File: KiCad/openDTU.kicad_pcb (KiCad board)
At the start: 4 copper layers, 40 x 50 mm, 54 parts, among them J1 USB_C_Receptacle_USB2.0, J2 Conn_Coaxial, J3 Micro_SD_Card, J4 Conn_02x05_Counter_Clockwise, Q1 BC817, Q2 BC817, SW1 SW_Push, SW2 SW_Push, U1 CH340C, U3 ESP32-WROOM-32, U4 nRF24L01P, U5 NCP1117-3.3_SOT223, Y1 16 MHz

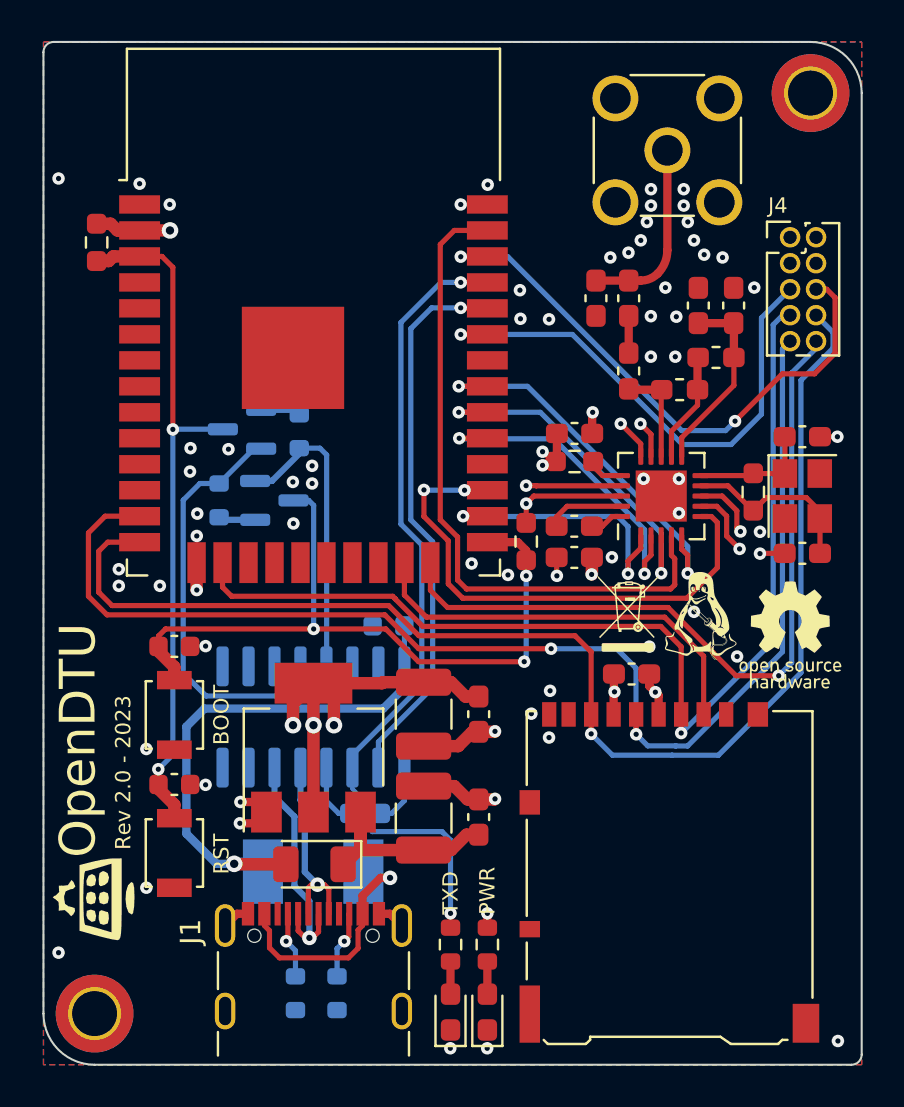
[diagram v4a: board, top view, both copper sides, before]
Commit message: first batch of smt variant ordered
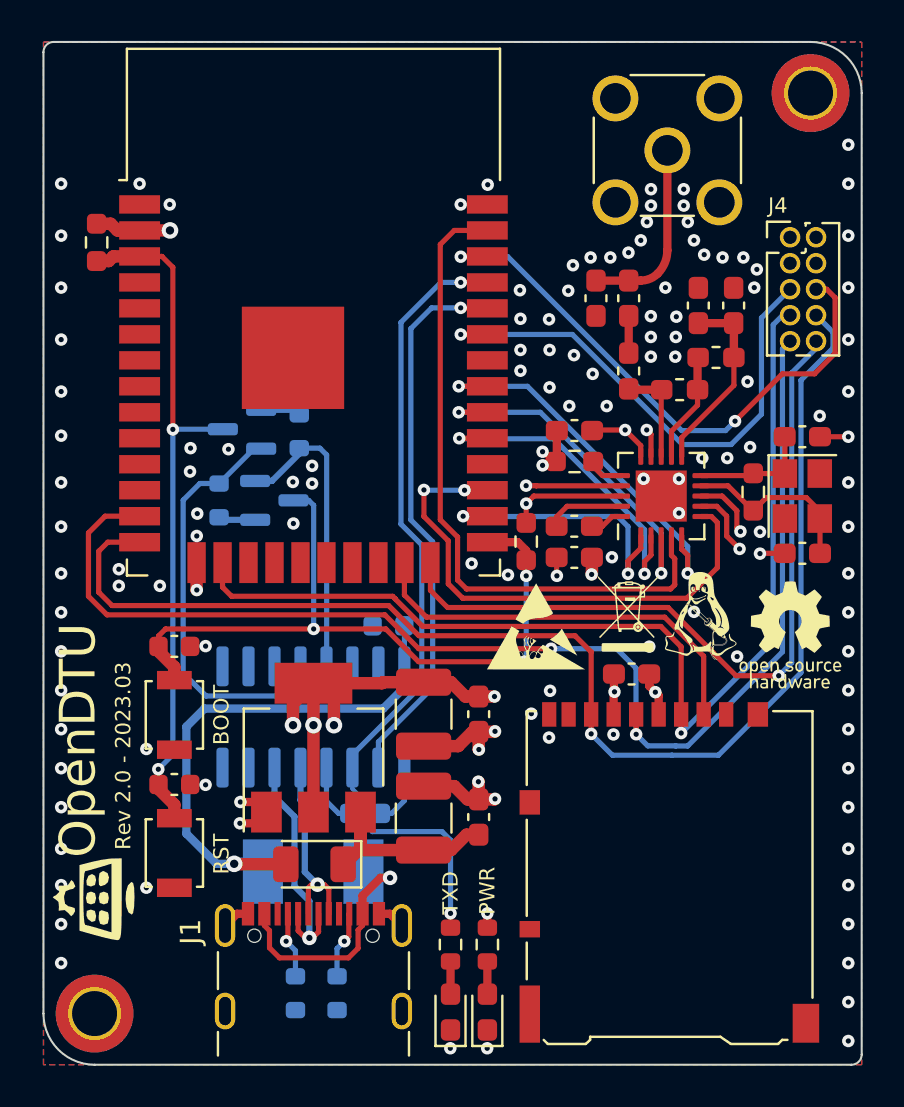
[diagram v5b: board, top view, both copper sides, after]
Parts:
- added G***: LOGO, LOGO, F.Cu at (149.6, 96.6)
- added REF**: KiCad-Logo2_6mm_SilkScreen, Symbol:KiCad-Logo2_6mm_SilkScreen, B.Cu at (154.9, 110.2)
- moved C3 0.14 mm to (151.5, 87.0), turned to 180 degrees
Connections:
- R1 pad 1: +3.3V -> GND
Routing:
- net GND: track 34.9 -> 38.8 mm, vias 72 -> 133
- net +3.3V: track 41.2 -> 40.3 mm, vias 12 -> 11
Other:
- board text added: "Rev 2.0 - 2023.03"
- board text removed: "Rev 2.0 - 2023"

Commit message: fixing bug with wrong voltage at USB-Seriell Interface IC
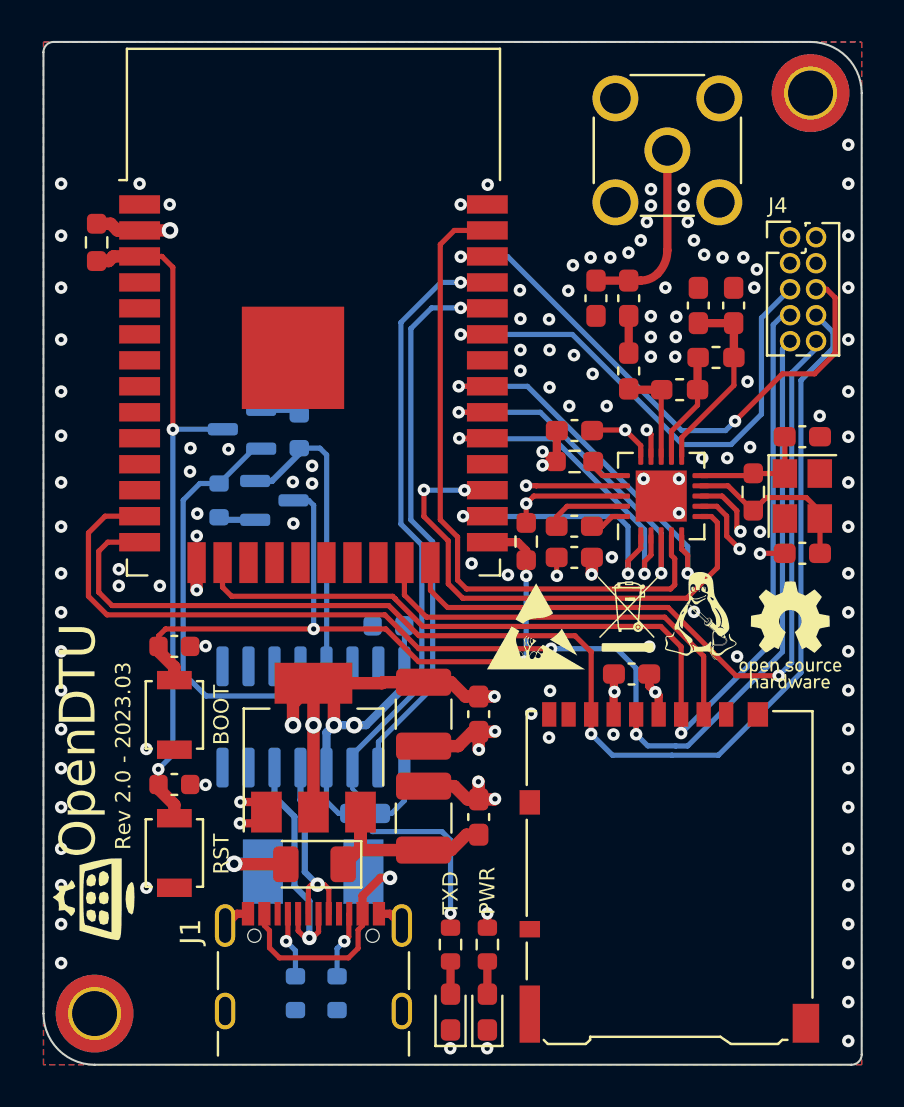
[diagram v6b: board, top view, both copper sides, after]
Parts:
- removed the REF** at (154.9, 110.2)
- C3: value 10nF -> 1nF
- D2: value LED -> SMLEN3EC8TT86
- R7: value 10k -> 100
- R8: value 10k -> 300
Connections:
- C15 pad 1: Net-(C15-Pad1) -> +3.3V
- C16 pad 1: VBUS -> +3.3V
- U1 pad 16: VBUS -> +3.3V
- U1 pad 4: Net-(C15-Pad1) -> +3.3V
- U4 pad 21: GND -> (no net)
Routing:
- net VBUS: track 27.8 -> 4.10 mm
- net +3.3V: track 40.3 -> 52.8 mm, vias 11 -> 12
- net Net-(C15-Pad1): track 3.01 -> 0.00 mm
- net GND: track 38.8 -> 37.4 mm
